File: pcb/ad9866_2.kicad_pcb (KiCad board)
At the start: 4 copper layers, 50 x 50 mm, 113 parts, among them CN1 MEC6-140_CONNECTOR_BEMICRO, CON1 USB-MICRO-B, P1 CONN_2, P10 CONN_1, P2 CONN_10X2, P3 CONN_1, P4 CONN_5X2, P5 CONN_1, P5V0 CONN_1, P6 Coaxial_Connector, P7 Coaxial_Connector, P8 CONN_2, P9 CONN_1, Q1 Si2301, T1 TRANSF_ADT2, T2 TRANSF_ADT8, U1 NCP1117ST33T3G, U2 NCP1117ST33T3G, U3 Si510, U4 AD9866BCPZ, U5 NCP1117ST33T3G, U6 25AA02E48T-I/OT

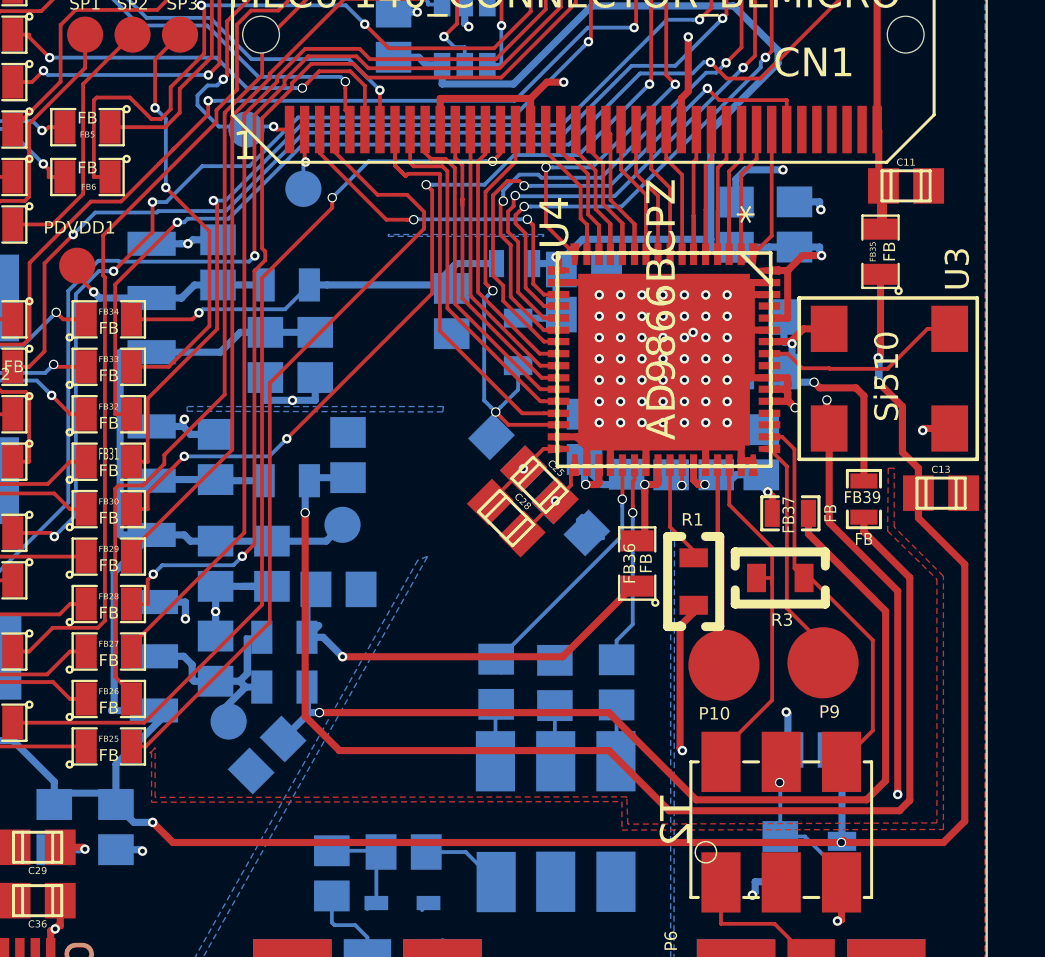
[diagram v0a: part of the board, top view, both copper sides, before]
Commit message: Special attention to the routing of CLKOUT1, added more ground plane.
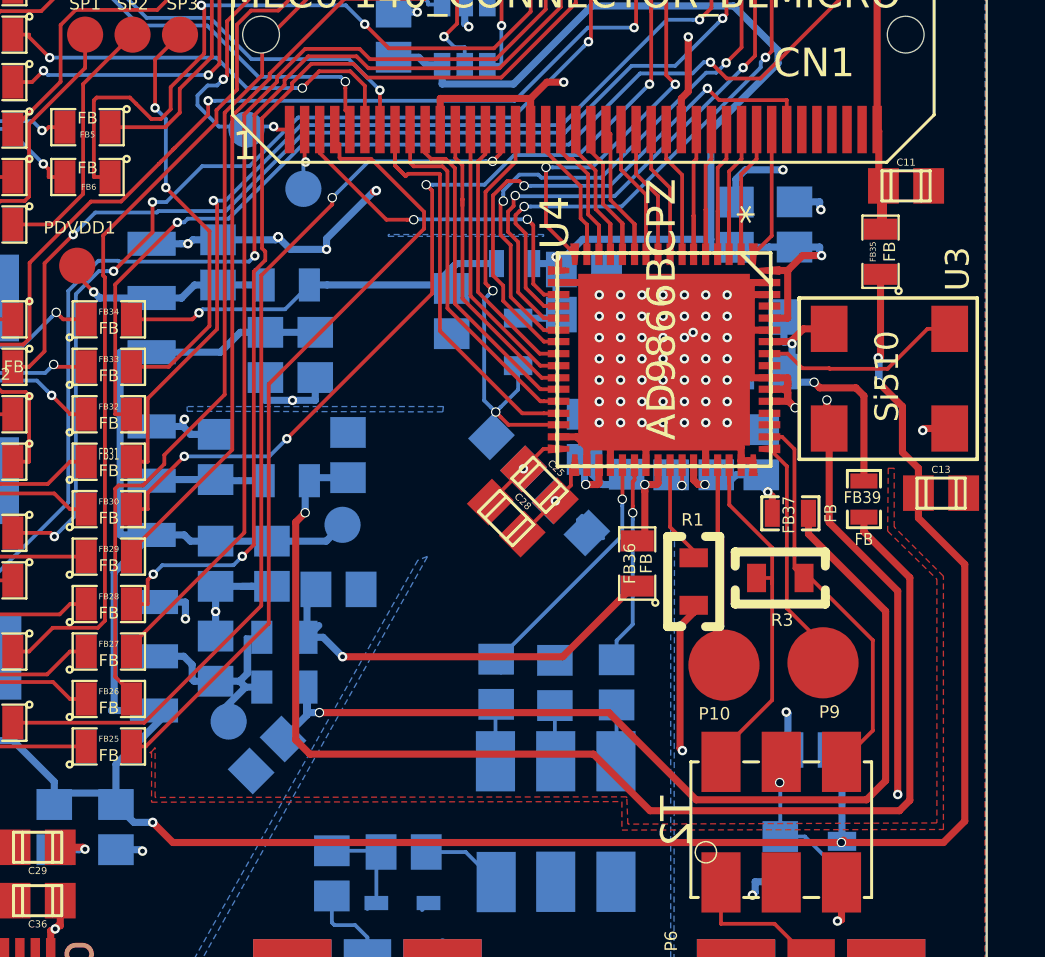
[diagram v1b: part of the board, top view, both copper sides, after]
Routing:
- net GND: track 138.0 -> 146.4 mm, vias 81 -> 85
- net Net-(C41-Pad1): track 51.9 -> 53.1 mm

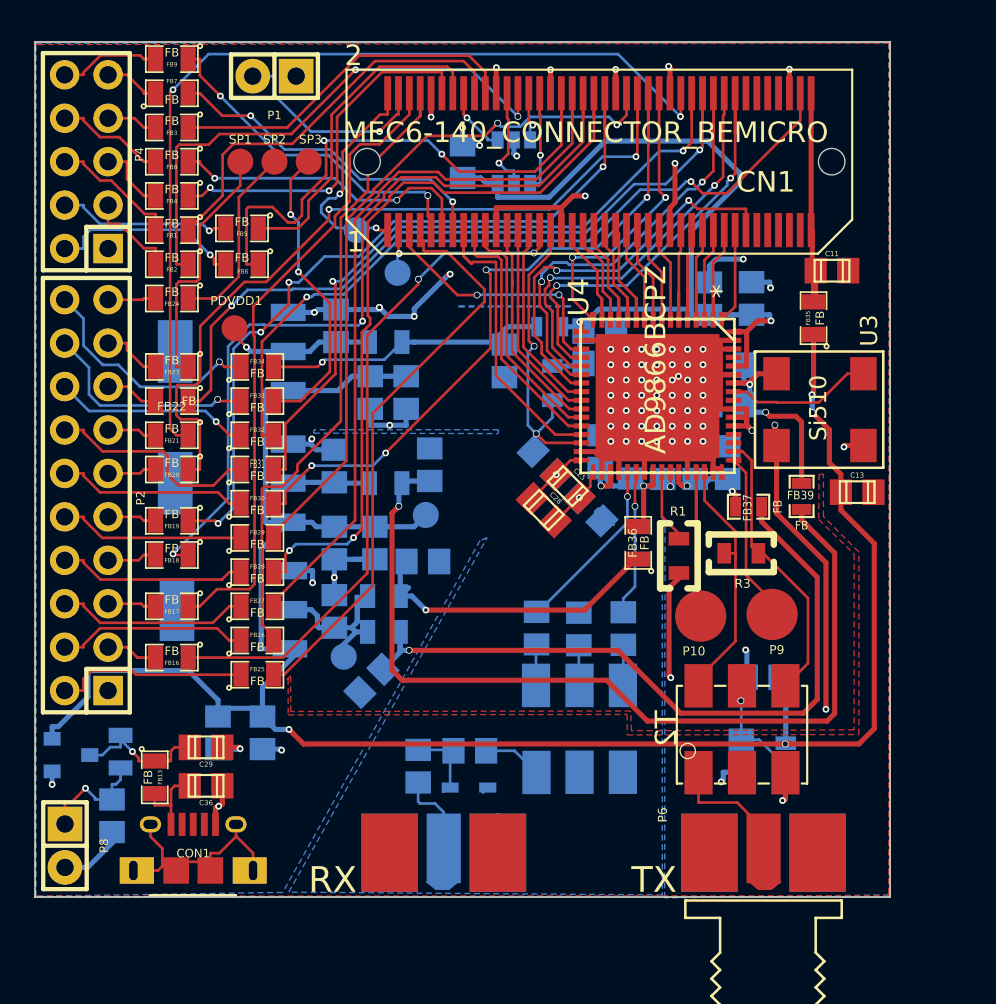
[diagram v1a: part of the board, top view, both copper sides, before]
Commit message: Removed a few 90 degree corners, cleaned up a few traces.
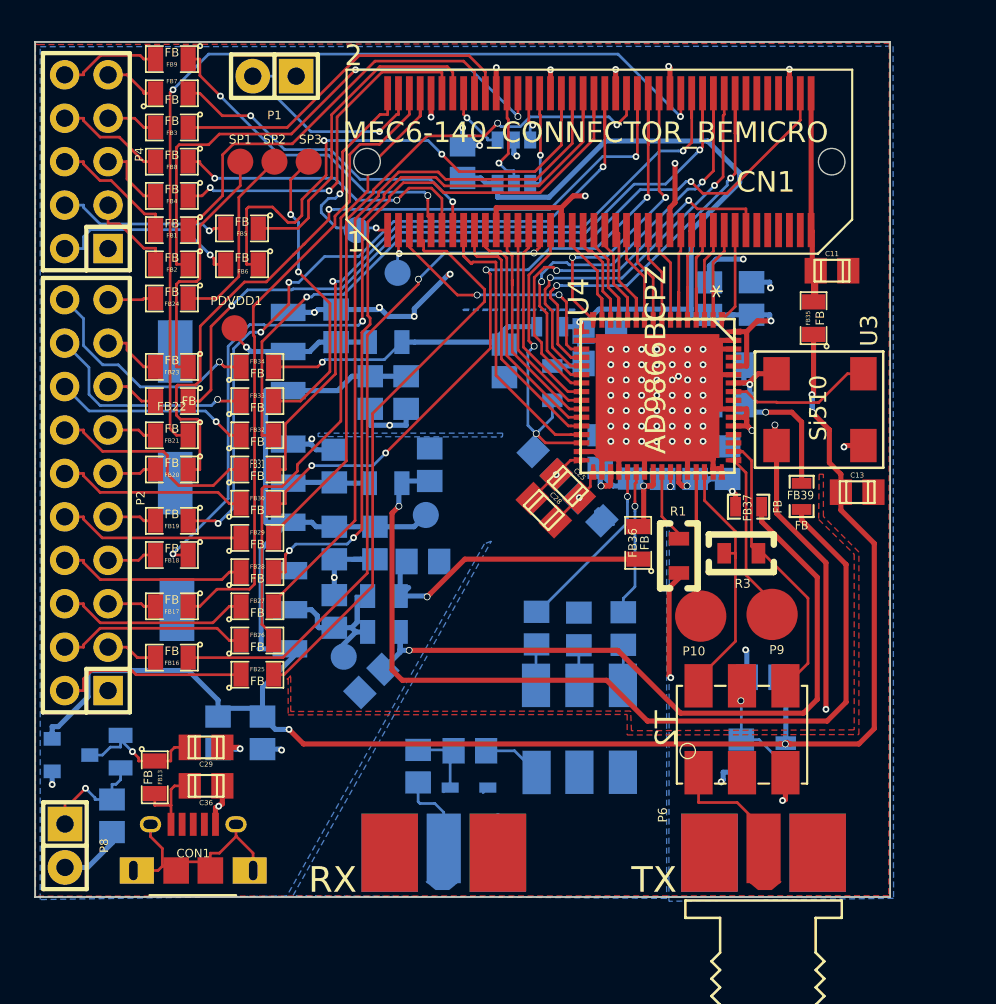
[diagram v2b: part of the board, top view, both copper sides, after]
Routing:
- net GND: track 146.4 -> 144.3 mm, vias 85 -> 84
- net Net-(C22-Pad1): track 19.4 -> 18.8 mm
- net Net-(C41-Pad1): track 53.1 -> 53.6 mm
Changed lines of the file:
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@@
     (area 122.064829 34.761469 1159.970001 93.0483)
     (thickness 1.6)
-    (drawings 7)
-    (tracks 1769)
+    (drawings 8)
+    (tracks 1765)
     (zones 0)
     (modules 113)
@@
     (zone_45_only no)
     (trace_min 0.1524)
-    (segment_width 2)
+    (segment_width 0.3)
     (edge_width 0.1)
     (via_size 0.4)
@@
     )
   )
+  (gr_line (start 150.375 50.45) (end 156.025 50.45) (angle 90) (layer B.SilkS) (width 0.3))
   (gr_text "Hermes-Lite\nv 1.1\nKL7NA" (at 158.242 77.216) (layer B.SilkS)
     (effects (font (size 0.5 0.5) (thickness 0.125)) (justify mirror))
@@
   (segment (start 159.65 53.95) (end 161.4 55.7) (width 0.3) (layer F.Cu) (net 2))
   (segment (start 152.06484 80.23498) (end 152.06484 82.41) (width 0.3) (layer B.Cu) (net 2))
-  (via (at 141.2283 66.625) (size 0.4) (layers F.Cu B.Cu) (net 2))
   (via (at 168.7101 79.3607) (size 0.4) (layers F.Cu B.Cu) (net 2))
   (via (at 126.0002 78.4225) (size 0.4) (layers F.Cu B.Cu) (net 2))
@@
   (via (at 141.3344 50.814) (size 0.4) (layers F.Cu B.Cu) (net 2))
   (via (at 162.4223 42.0958) (size 0.4) (layers F.Cu B.Cu) (net 2))
-  (segment (start 139.902 65.914) (end 141.2283 65.914) (width 0.3) (layer B.Cu) (net 2))
-  (segment (start 141.2283 65.914) (end 141.2283 66.625) (width 0.3) (layer B.Cu) (net 2))
   (segment (start 168.88 77.73) (end 168.88 79.3103) (width 0.3) (layer F.Cu) (net 2))
   (segment (start 168.7605 79.3103) (end 168.88 79.3103) (width 0.3) (layer F.Cu) (net 2))
@@
   (segment (start 158.6568 60.9022) (end 158.596788 60.962212) (width 0.3) (layer F.Cu) (net 6))
   (segment (start 158.382842 60.962212) (end 158.1 60.962212) (width 0.3) (layer F.Cu) (net 6))
+  (segment (start 169.825 60.813) (end 169.825 57.225482) (width 0.3) (layer F.Cu) (net 7))
+  (segment (start 169.249518 56.65) (end 167.725 56.65) (width 0.3) (layer F.Cu) (net 7))
+  (segment (start 169.825 57.225482) (end 169.249518 56.65) (width 0.3) (layer F.Cu) (net 7))
   (via (at 166.797 55.0252) (size 0.4) (layers F.Cu B.Cu) (net 7))
   (segment (start 166.797 56.3855) (end 166.797 55.0252) (width 0.3) (layer B.Cu) (net 7))
@@
   (segment (start 166.452 56.4649) (end 166.4525 56.4644) (width 0.3) (layer B.Cu) (net 7))
   (segment (start 166.9025 56.65) (end 166.4525 56.2) (width 0.3) (layer B.Cu) (net 7))
-  (segment (start 169.825 57.225482) (end 169.487259 56.887741) (width 0.3) (layer F.Cu) (net 7))
-  (segment (start 169.487259 56.887741) (end 167.962741 56.887741) (width 0.3) (layer F.Cu) (net 7))
-  (segment (start 167.962741 56.887741) (end 167.725 56.65) (width 0.3) (layer F.Cu) (net 7))
   (segment (start 167.725 56.65) (end 166.9025 56.65) (width 0.3) (layer B.Cu) (net 7))
   (via (at 167.725 56.65) (size 0.4) (drill 0.3) (layers F.Cu B.Cu) (net 7))
-  (segment (start 169.825 60.813) (end 169.825 57.225482) (width 0.3) (layer F.Cu) (net 7))
   (segment (start 156.8 70.2775) (end 156.8 72.59) (width 0.16) (layer B.Cu) (net 8))
   (segment (start 156.8 72.59) (end 156.835 72.625) (width 0.16) (layer B.Cu) (net 8))
@@
   (segment (start 142.14 41.6136) (end 144.306411 43.780011) (width 0.16) (layer B.Cu) (net 64))
   (segment (start 147.969 45.1908) (end 147.969 44.262852) (width 0.16) (layer F.Cu) (net 64))
+  (segment (start 156.955 52.9568) (end 156.3378 52.9568) (width 0.16) (layer F.Cu) (net 65))
+  (segment (start 156.3378 52.9568) (end 156.075 52.694) (width 0.16) (layer F.Cu) (net 65))
+  (segment (start 156.075 52.694) (end 156.075 50.218815) (width 0.16) (layer F.Cu) (net 65))
+  (segment (start 156.075 50.218815) (end 155.83962 49.983435) (width 0.16) (layer F.Cu) (net 65))
+  (segment (start 155.83962 49.983435) (end 155.639621 49.783436) (width 0.16) (layer F.Cu) (net 65))
   (segment (start 149.7 49.8) (end 150.567158 49.8) (width 0.16) (layer F.Cu) (net 65))
   (segment (start 150.567158 49.8) (end 150.85 49.8) (width 0.16) (layer F.Cu) (net 65))
@@
   (segment (start 146.8875 46.6196) (end 146.8875 46) (width 0.16) (layer F.Cu) (net 65))
   (segment (start 146.888 46.6201) (end 146.8875 46.6196) (width 0.16) (layer F.Cu) (net 65))
-  (segment (start 156.3378 52.9568) (end 155.889757 52.508757) (width 0.16) (layer F.Cu) (net 65))
-  (segment (start 155.83962 49.983435) (end 155.639621 49.783436) (width 0.16) (layer F.Cu) (net 65))
-  (segment (start 155.889757 52.508757) (end 155.889757 50.033572) (width 0.16) (layer F.Cu) (net 65))
-  (segment (start 156.955 52.9568) (end 156.3378 52.9568) (width 0.16) (layer F.Cu) (net 65))
   (via (at 155.639621 49.783436) (size 0.4) (drill 0.3) (layers F.Cu B.Cu) (net 65))
-  (segment (start 155.889757 50.033572) (end 155.83962 49.983435) (width 0.16) (layer F.Cu) (net 65))
   (via (at 150.85 49.8) (size 0.4) (drill 0.3) (layers F.Cu B.Cu) (net 65))
   (segment (start 155.639621 49.783436) (end 150.866564 49.783436) (width 0.16) (layer B.Cu) (net 65))
@@
   (segment (start 170.525 48.4975) (end 170.6475 48.375) (width 0.3) (layer F.Cu) (net 123))
   (segment (start 170.525 50.1975) (end 170.525 48.4975) (width 0.3) (layer F.Cu) (net 123))
-  (segment (start 160.27 65.2425) (end 160.1075 65.2425) (width 0.3) (layer F.Cu) (net 124))
-  (segment (start 160.1075 65.2425) (end 157.13 68.22) (width 0.3) (layer F.Cu) (net 124))
-  (segment (start 157.13 68.22) (end 147.85 68.22) (width 0.3) (layer F.Cu) (net 124))
-  (via (at 147.85 68.22) (size 0.4) (layers F.Cu B.Cu) (net 124))
-  (segment (start 147.85 68.22) (end 147.03 67.4) (width 0.3) (layer B.Cu) (net 124))
-  (segment (start 147.03 67.4) (end 146.3525 67.4) (width 0.3) (layer B.Cu) (net 124))
+  (segment (start 148.124999 67.250001) (end 147.925 67.45) (width 0.3) (layer F.Cu) (net 124))
+  (segment (start 150.1325 65.2425) (end 148.124999 67.250001) (width 0.3) (layer F.Cu) (net 124))
+  (segment (start 160.27 65.2425) (end 150.1325 65.2425) (width 0.3) (layer F.Cu) (net 124))
+  (segment (start 147.875 67.4) (end 147.925 67.45) (width 0.3) (layer B.Cu) (net 124))
+  (segment (start 146.3525 67.4) (end 147.875 67.4) (width 0.3) (layer B.Cu) (net 124))
+  (via (at 147.925 67.45) (size 0.4) (drill 0.3) (layers F.Cu B.Cu) (net 124))
   (segment (start 146.7275 65.38) (end 146.7275 65.7475) (width 0.3) (layer B.Cu) (net 124))
   (segment (start 146.3525 67.4) (end 146.3525 65.755) (width 0.3) (layer B.Cu) (net 124))
@@
   (segment (start 146.875 70.575) (end 146.375 70.575) (width 0.3) (layer B.Cu) (net 125))
   (segment (start 169.825 62.337) (end 169.825 62.9545) (width 0.3) (layer F.Cu) (net 126))
-  (segment (start 169.825 62.9545) (end 171.760001 64.889501) (width 0.3) (layer F.Cu) (net 126))
-  (segment (start 171.760001 64.889501) (end 171.760001 74.269801) (width 0.3) (layer F.Cu) (net 126))
-  (segment (start 171.760001 74.269801) (end 171.319792 74.71001) (width 0.3) (layer F.Cu) (net 126))
+  (segment (start 172.425 73.604802) (end 171.319792 74.71001) (width 0.3) (layer F.Cu) (net 126))
+  (segment (start 169.825 62.9545) (end 172.425 65.5545) (width 0.3) (layer F.Cu) (net 126))
+  (segment (start 172.425 65.5545) (end 172.425 73.604802) (width 0.3) (layer F.Cu) (net 126))
   (segment (start 171.319792 74.71001) (end 160.81001 74.71001) (width 0.3) (layer F.Cu) (net 126))
+  (segment (start 146.475 72.325) (end 145.875 71.725) (width 0.3) (layer F.Cu) (net 126))
   (segment (start 160.81001 74.71001) (end 158.425 72.325) (width 0.3) (layer F.Cu) (net 126))
   (segment (start 158.425 72.325) (end 146.475 72.325) (width 0.3) (layer F.Cu) (net 126))
-  (segment (start 146.475 72.325) (end 145.875 71.725) (width 0.3) (layer F.Cu) (net 126))
   (segment (start 145.875 71.725) (end 145.875 62.55) (width 0.3) (layer F.Cu) (net 126))
   (segment (start 145.875 62.55) (end 146.275 62.15) (width 0.3) (layer F.Cu) (net 126))
@@
     (polygon
       (pts
-        (xy 174.95 84.875) (xy 161.815 85.05) (xy 161.84 62.975) (xy 161.68 62.83) (xy 161.68 84.88)
-        (xy 139.835 84.715) (xy 151.435 63.99) (xy 151.025 64.15) (xy 139.48 84.73) (xy 125.05 84.95)
-        (xy 125.05 35.075) (xy 174.925 35.05)
+        (xy 175.2 85.075) (xy 162.065 85.25) (xy 162.09 63.175) (xy 161.93 63.03) (xy 161.93 85.08)
+        (xy 140.085 84.915) (xy 151.685 64.19) (xy 151.275 64.35) (xy 139.73 84.93) (xy 125.3 85.15)
+        (xy 125.3 35.275) (xy 175.175 35.25)
       )
     )
     (polygon
-      (pts        (xy 152.1 57.675) (xy 141.3 57.675) (xy 141.3 57.875) (xy 152.075 57.9)
+      (pts        (xy 152.35 57.875) (xy 141.55 57.875) (xy 141.55 58.075) (xy 152.325 58.1)
       )
     )
     (polygon
-      (pts        (xy 149.775 50.5) (xy 156.325 50.5) (xy 156.325 50.425) (xy 149.775 50.425)
+      (pts        (xy 150.025 50.7) (xy 156.575 50.7) (xy 156.575 50.625) (xy 150.025 50.625)
       )
     )

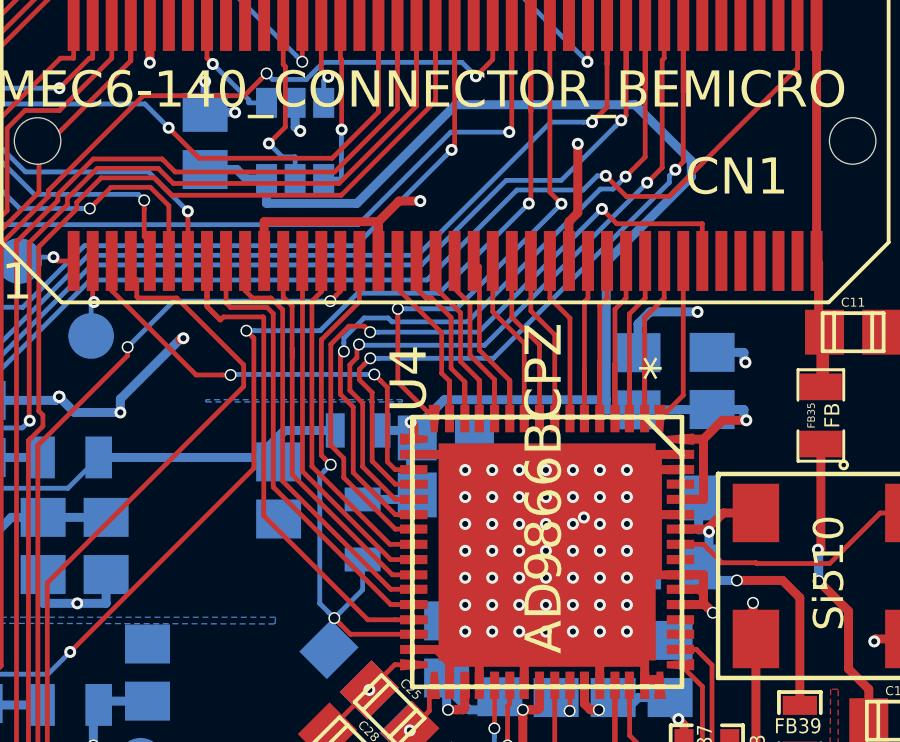
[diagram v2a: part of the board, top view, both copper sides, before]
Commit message: Removed the solder mask to make installing copper tape shields.
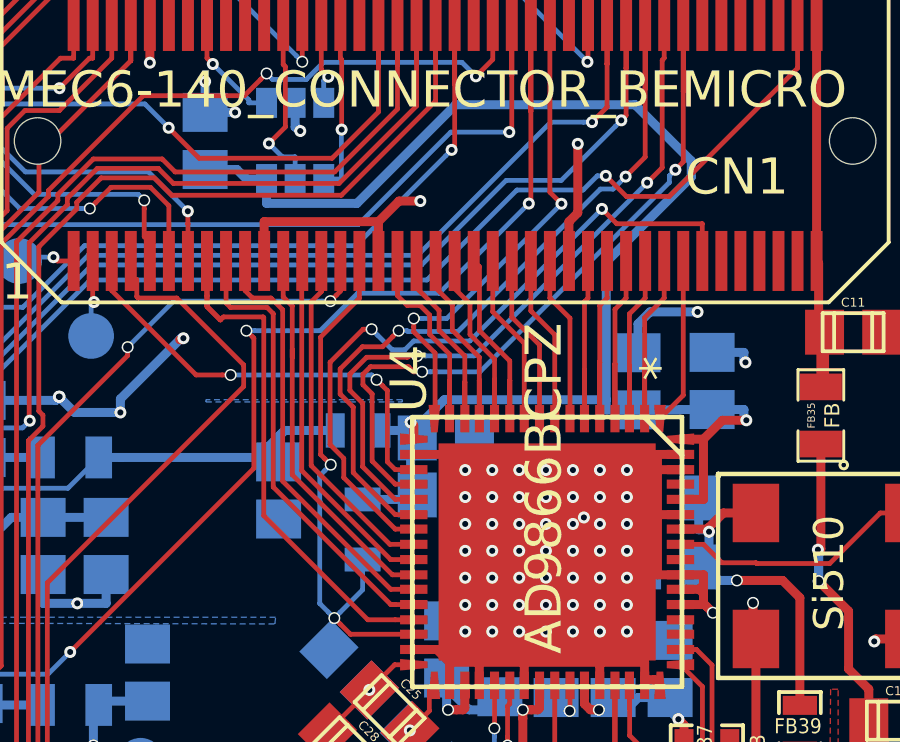
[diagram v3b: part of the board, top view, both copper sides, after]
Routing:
- net Net-(CN1-Pad52): track 17.3 -> 16.4 mm
- net /SCK: track 26.8 -> 26.2 mm
